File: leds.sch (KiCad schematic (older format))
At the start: 26 parts

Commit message: Use 0805 for all capacitors and resistors.
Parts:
- C? (x9): footprint (none) -> Capacitor_SMD:C_0805_2012Metric_Pad1.15x1.40mm_HandSolder; symbol Device:C -> Drone:CAP
- R? (x12): footprint (none) -> Resistor_SMD:R_0805_2012Metric_Pad1.15x1.40mm_HandSolder; symbol Device:R -> Drone:RES
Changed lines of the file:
@@
 	3200 4850 2950 4850
 $Comp
-L Device:R R?
+L Drone:RES R?
 U 1 1 5E39412E
 P 2800 5250
@@
 F 0 "R?" V 2850 5350 50  0000 L CNN
 F 1 "130" V 2870 5205 50  0000 L CNN
-F 2 "" V 2730 5250 50  0001 C CNN
+F 2 "Resistor_SMD:R_0805_2012Metric_Pad1.15x1.40mm_HandSolder" V 2730 5250 50  0001 C CNN
 F 3 "~" H 2800 5250 50  0001 C CNN
 	1    2800 5250
@@
 $EndComp
 $Comp
-L Device:R R?
+L Drone:RES R?
 U 1 1 5E394128
 P 2800 4850
@@
 F 0 "R?" V 2850 4950 50  0000 L CNN
 F 1 "56" V 2870 4805 50  0000 L CNN
-F 2 "" V 2730 4850 50  0001 C CNN
+F 2 "Resistor_SMD:R_0805_2012Metric_Pad1.15x1.40mm_HandSolder" V 2730 4850 50  0001 C CNN
 F 3 "~" H 2800 4850 50  0001 C CNN
 	1    2800 4850
@@
 $EndComp
 $Comp
-L Device:R R?
+L Drone:RES R?
 U 1 1 5E394122
 P 2800 5050
@@
 F 0 "R?" V 2850 5150 50  0000 L CNN
 F 1 "56" V 2870 5005 50  0000 L CNN
-F 2 "" V 2730 5050 50  0001 C CNN
+F 2 "Resistor_SMD:R_0805_2012Metric_Pad1.15x1.40mm_HandSolder" V 2730 5050 50  0001 C CNN
 F 3 "~" H 2800 5050 50  0001 C CNN
 	1    2800 5050
@@
 	10400 2000 10500 2100
 $Comp
-L Device:C C?
+L Drone:CAP C?
 U 1 1 5E322DC6
 P 8600 3250
@@
 F 0 "C?" H 8715 3296 50  0000 L CNN
 F 1 "100nF" H 8715 3205 50  0000 L CNN
-F 2 "" H 8638 3100 50  0001 C CNN
+F 2 "Capacitor_SMD:C_0805_2012Metric_Pad1.15x1.40mm_HandSolder" H 8638 3100 50  0001 C CNN
 F 3 "~" H 8600 3250 50  0001 C CNN
 	1    8600 3250
@@
 GND
 $Comp
-L Device:C C?
+L Drone:CAP C?
 U 1 1 5E41CE8E
 P 1550 5050
@@
 F 0 "C?" H 1665 5096 50  0000 L CNN
 F 1 "10u" H 1665 5005 50  0000 L CNN
-F 2 "" H 1588 4900 50  0001 C CNN
+F 2 "Capacitor_SMD:C_0805_2012Metric_Pad1.15x1.40mm_HandSolder" H 1588 4900 50  0001 C CNN
 F 3 "~" H 1550 5050 50  0001 C CNN
 	1    1550 5050
@@
 $EndComp
 $Comp
-L Device:C C?
+L Drone:CAP C?
 U 1 1 5E423672
 P 1100 5050
@@
 F 0 "C?" H 1215 5096 50  0000 L CNN
 F 1 "100n" H 1215 5005 50  0000 L CNN
-F 2 "" H 1138 4900 50  0001 C CNN
+F 2 "Capacitor_SMD:C_0805_2012Metric_Pad1.15x1.40mm_HandSolder" H 1138 4900 50  0001 C CNN
 F 3 "~" H 1100 5050 50  0001 C CNN
 	1    1100 5050
@@
 	5600 4850 5350 4850
 $Comp
-L Device:R R?
+L Drone:RES R?
 U 1 1 5E35DA90
 P 5200 5250
@@
 F 0 "R?" V 5250 5350 50  0000 L CNN
 F 1 "130" V 5270 5205 50  0000 L CNN
-F 2 "" V 5130 5250 50  0001 C CNN
+F 2 "Resistor_SMD:R_0805_2012Metric_Pad1.15x1.40mm_HandSolder" V 5130 5250 50  0001 C CNN
 F 3 "~" H 5200 5250 50  0001 C CNN
 	1    5200 5250
@@
 $EndComp
 $Comp
-L Device:R R?
+L Drone:RES R?
 U 1 1 5E35DA96
 P 5200 4850
@@
 F 0 "R?" V 5250 4950 50  0000 L CNN
 F 1 "56" V 5270 4805 50  0000 L CNN
-F 2 "" V 5130 4850 50  0001 C CNN
+F 2 "Resistor_SMD:R_0805_2012Metric_Pad1.15x1.40mm_HandSolder" V 5130 4850 50  0001 C CNN
 F 3 "~" H 5200 4850 50  0001 C CNN
 	1    5200 4850
@@
 $EndComp
 $Comp
-L Device:R R?
+L Drone:RES R?
 U 1 1 5E35DA9C
 P 5200 5050
@@
 F 0 "R?" V 5250 5150 50  0000 L CNN
 F 1 "56" V 5270 5005 50  0000 L CNN
-F 2 "" V 5130 5050 50  0001 C CNN
+F 2 "Resistor_SMD:R_0805_2012Metric_Pad1.15x1.40mm_HandSolder" V 5130 5050 50  0001 C CNN
 F 3 "~" H 5200 5050 50  0001 C CNN
 	1    5200 5050
@@
 GND
 $Comp
-L Device:C C?
+L Drone:CAP C?
 U 1 1 5E35DAAA
 P 3950 5050
@@
 F 0 "C?" H 4065 5096 50  0000 L CNN
 F 1 "10u" H 4065 5005 50  0000 L CNN
-F 2 "" H 3988 4900 50  0001 C CNN
+F 2 "Capacitor_SMD:C_0805_2012Metric_Pad1.15x1.40mm_HandSolder" H 3988 4900 50  0001 C CNN
 F 3 "~" H 3950 5050 50  0001 C CNN
 	1    3950 5050
@@
 $EndComp
 $Comp
-L Device:C C?
+L Drone:CAP C?
 U 1 1 5E35DAB0
 P 3500 5050
@@
 F 0 "C?" H 3615 5096 50  0000 L CNN
 F 1 "100n" H 3615 5005 50  0000 L CNN
-F 2 "" H 3538 4900 50  0001 C CNN
+F 2 "Capacitor_SMD:C_0805_2012Metric_Pad1.15x1.40mm_HandSolder" H 3538 4900 50  0001 C CNN
 F 3 "~" H 3500 5050 50  0001 C CNN
 	1    3500 5050
@@
 	8000 4850 7750 4850
 $Comp
-L Device:R R?
+L Drone:RES R?
 U 1 1 5E363A4B
 P 7600 5250
@@
 F 0 "R?" V 7650 5350 50  0000 L CNN
 F 1 "130" V 7670 5205 50  0000 L CNN
-F 2 "" V 7530 5250 50  0001 C CNN
+F 2 "Resistor_SMD:R_0805_2012Metric_Pad1.15x1.40mm_HandSolder" V 7530 5250 50  0001 C CNN
 F 3 "~" H 7600 5250 50  0001 C CNN
 	1    7600 5250
@@
 $EndComp
 $Comp
-L Device:R R?
+L Drone:RES R?
 U 1 1 5E363A51
 P 7600 4850
@@
 F 0 "R?" V 7650 4950 50  0000 L CNN
 F 1 "56" V 7670 4805 50  0000 L CNN
-F 2 "" V 7530 4850 50  0001 C CNN
+F 2 "Resistor_SMD:R_0805_2012Metric_Pad1.15x1.40mm_HandSolder" V 7530 4850 50  0001 C CNN
 F 3 "~" H 7600 4850 50  0001 C CNN
 	1    7600 4850
@@
 $EndComp
 $Comp
-L Device:R R?
+L Drone:RES R?
 U 1 1 5E363A57
 P 7600 5050
@@
 F 0 "R?" V 7650 5150 50  0000 L CNN
 F 1 "56" V 7670 5005 50  0000 L CNN
-F 2 "" V 7530 5050 50  0001 C CNN
+F 2 "Resistor_SMD:R_0805_2012Metric_Pad1.15x1.40mm_HandSolder" V 7530 5050 50  0001 C CNN
 F 3 "~" H 7600 5050 50  0001 C CNN
 	1    7600 5050
@@
 GND
 $Comp
-L Device:C C?
+L Drone:CAP C?
 U 1 1 5E363A65
 P 6350 5050
@@
 F 0 "C?" H 6465 5096 50  0000 L CNN
 F 1 "10u" H 6465 5005 50  0000 L CNN
-F 2 "" H 6388 4900 50  0001 C CNN
+F 2 "Capacitor_SMD:C_0805_2012Metric_Pad1.15x1.40mm_HandSolder" H 6388 4900 50  0001 C CNN
 F 3 "~" H 6350 5050 50  0001 C CNN
 	1    6350 5050
@@
 $EndComp
 $Comp
-L Device:C C?
+L Drone:CAP C?
 U 1 1 5E363A6B
 P 5900 5050
@@
 F 0 "C?" H 6015 5096 50  0000 L CNN
 F 1 "100n" H 6015 5005 50  0000 L CNN
-F 2 "" H 5938 4900 50  0001 C CNN
+F 2 "Capacitor_SMD:C_0805_2012Metric_Pad1.15x1.40mm_HandSolder" H 5938 4900 50  0001 C CNN
 F 3 "~" H 5900 5050 50  0001 C CNN
 	1    5900 5050
@@
 	10400 4850 10150 4850
 $Comp
-L Device:R R?
+L Drone:RES R?
 U 1 1 5E370DE6
 P 10000 5250
@@
 F 0 "R?" V 10050 5350 50  0000 L CNN
 F 1 "130" V 10070 5205 50  0000 L CNN
-F 2 "" V 9930 5250 50  0001 C CNN
+F 2 "Resistor_SMD:R_0805_2012Metric_Pad1.15x1.40mm_HandSolder" V 9930 5250 50  0001 C CNN
 F 3 "~" H 10000 5250 50  0001 C CNN
 	1    10000 5250
@@
 $EndComp
 $Comp
-L Device:R R?
+L Drone:RES R?
 U 1 1 5E370DEC
 P 10000 4850
@@
 F 0 "R?" V 10050 4950 50  0000 L CNN
 F 1 "56" V 10070 4805 50  0000 L CNN
-F 2 "" V 9930 4850 50  0001 C CNN
+F 2 "Resistor_SMD:R_0805_2012Metric_Pad1.15x1.40mm_HandSolder" V 9930 4850 50  0001 C CNN
 F 3 "~" H 10000 4850 50  0001 C CNN
 	1    10000 4850
@@
 $EndComp
 $Comp
-L Device:R R?
+L Drone:RES R?
 U 1 1 5E370DF2
 P 10000 5050
@@
 F 0 "R?" V 10050 5150 50  0000 L CNN
 F 1 "56" V 10070 5005 50  0000 L CNN
-F 2 "" V 9930 5050 50  0001 C CNN
+F 2 "Resistor_SMD:R_0805_2012Metric_Pad1.15x1.40mm_HandSolder" V 9930 5050 50  0001 C CNN
 F 3 "~" H 10000 5050 50  0001 C CNN
 	1    10000 5050
@@
 GND
 $Comp
-L Device:C C?
+L Drone:CAP C?
 U 1 1 5E370E00
 P 8750 5050
@@
 F 0 "C?" H 8865 5096 50  0000 L CNN
 F 1 "10u" H 8865 5005 50  0000 L CNN
-F 2 "" H 8788 4900 50  0001 C CNN
+F 2 "Capacitor_SMD:C_0805_2012Metric_Pad1.15x1.40mm_HandSolder" H 8788 4900 50  0001 C CNN
 F 3 "~" H 8750 5050 50  0001 C CNN
 	1    8750 5050
@@
 $EndComp
 $Comp
-L Device:C C?
+L Drone:CAP C?
 U 1 1 5E370E06
 P 8300 5050
@@
 F 0 "C?" H 8415 5096 50  0000 L CNN
 F 1 "100n" H 8415 5005 50  0000 L CNN
-F 2 "" H 8338 4900 50  0001 C CNN
+F 2 "Capacitor_SMD:C_0805_2012Metric_Pad1.15x1.40mm_HandSolder" H 8338 4900 50  0001 C CNN
 F 3 "~" H 8300 5050 50  0001 C CNN
 	1    8300 5050

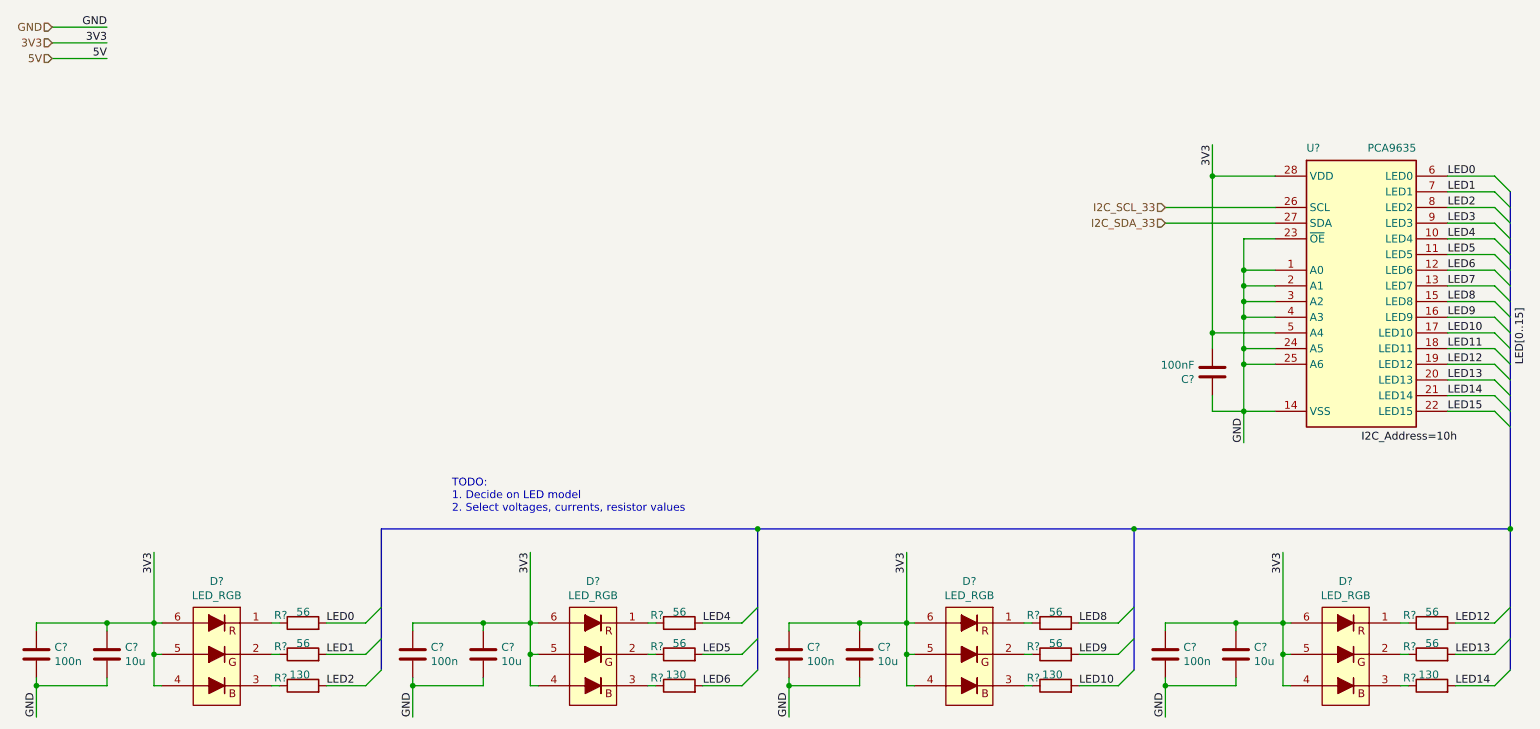
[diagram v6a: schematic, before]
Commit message: Update the LEDs and resistor values. Add TELEM2 connector for Pixhawk.
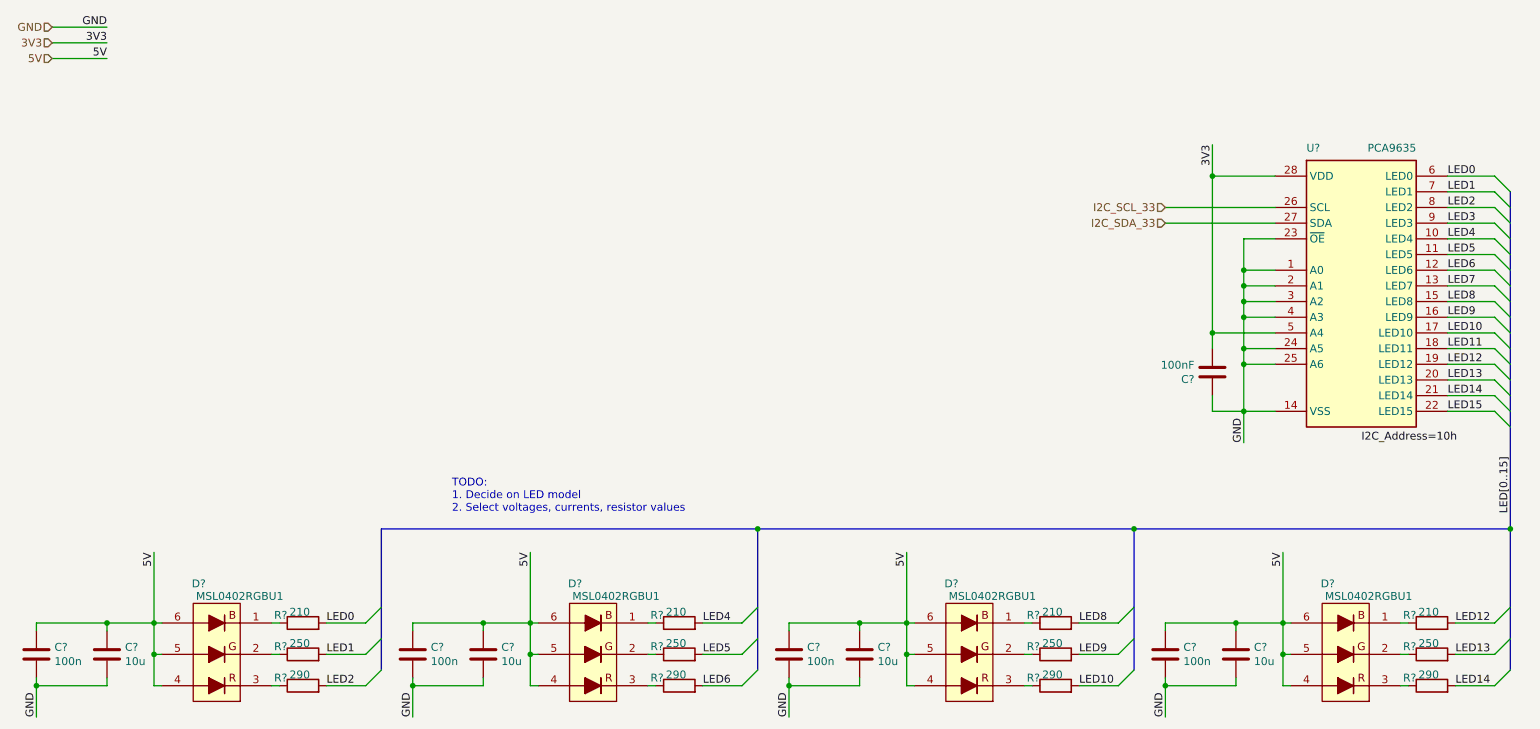
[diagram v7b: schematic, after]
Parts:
- removed D? (x4): LED_RGB, symbol Drone:LED_RGB
- removed R? (x3): 130, Resistor_SMD:R_0805_2012Metric_Pad1.15x1.40mm_HandSolder, symbol Drone:RES
- removed R? (x6): 56, Resistor_SMD:R_0805_2012Metric_Pad1.15x1.40mm_HandSolder, symbol Drone:RES
- added D? (x4): MSL0402RGBU1, Drone:MSL0402RGBU1, symbol Drone:MSL0402RGBU1
- added R? (x3): 290, Resistor_SMD:R_0805_2012Metric_Pad1.15x1.40mm_HandSolder, symbol Drone:RES
- added R? (x3): 210, Resistor_SMD:R_0805_2012Metric_Pad1.15x1.40mm_HandSolder, symbol Drone:RES
- added R? (x3): 250, Resistor_SMD:R_0805_2012Metric_Pad1.15x1.40mm_HandSolder, symbol Drone:RES
- R?: value 56 -> 250
- R?: value 56 -> 210
- R?: value 130 -> 290
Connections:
- net 3V3: no longer C?.1, C?.1, C?.1, C?.1, C?.1, C?.1, C?.1, C?.1
- net 5V: now also C?.1, C?.1, C?.1, C?.1, C?.1, C?.1, C?.1, C?.1, D?.4 (RA), D?.4 (RA), D?.4 (RA), D?.4 (RA), D?.5 (GA), D?.5 (GA), D?.5 (GA), D?.5 (GA), D?.6 (BA), D?.6 (BA), D?.6 (BA), D?.6 (BA)
- net LED10: now also R?.2
- net LED12: now also R?.2
- net LED13: now also R?.2
- net LED14: now also R?.2
- net LED4: now also R?.2
- net LED5: now also R?.2
- net LED6: now also R?.2
- net LED8: now also R?.2
- net LED9: now also R?.2
- net at R?.1: now also D?.1 (BK)
- net at R?.1: now also D?.2 (GK)
- net at R?.1: now also D?.3 (RK)
- new net: D?.1 (BK), R?.1 (x3)
- new net: D?.2 (GK), R?.1 (x3)
- new net: D?.3 (RK), R?.1 (x3)

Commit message: Minor fixes.
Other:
- note added: "7-bit Address: 0x10"
- note removed: "TODO:\n1. Decide on LED model\n2. Select voltages, currents, resistor values"
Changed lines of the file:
@@
 Wire Wire Line
 	8600 3000 9000 3000
-Text Label 9550 3700 0    50   ~ 0
-I2C_Address=10h
 Text HLabel 8300 2300 0    50   Input ~ 0
 I2C_SDA_33
@@
 	8600 3100 8600 3000
 Connection ~ 8600 3000
-Text Notes 3750 4150 0    50   ~ 0
-TODO:\n1. Decide on LED model\n2. Select voltages, currents, resistor values
 Wire Wire Line
 	2650 4850 2600 4850
@@
 	0    -1   -1   0
 $EndComp
+Text Notes 9200 3700 0    50   ~ 0
+7-bit Address: 0x10
 Wire Bus Line
 	3300 4250 3300 5150
